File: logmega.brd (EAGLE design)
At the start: 163.8 x 97.2 mm, 94 parts, among them IC1 LTC4412, IC2 4050D, IC3 ATMEGA2560-16AU, IC4 4050D, J1 POWER_JACKPTH, M0R1 ?K, M0R2 ?K, M1 FDG6342L, M1C1 ?uF, M1R1 ?K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

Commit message: begin 083_rev2
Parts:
- C11: value 100n -> 0.1uF
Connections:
- net VCC_SW_SHIELD1: no longer U$7.IOREF
- net VCC_SW_SHIELD2: now also U$7.IOREF
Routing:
- net VCC_SW_SHIELD1: track 109.2 -> 23.9 mm, vias 3 -> 0
- net VCC_SW_SHIELD2: track 16.0 -> 25.1 mm
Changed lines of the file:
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@@
 <text x="138.5825" y="22.2025" size="0.6096" layer="21">TM</text>
 <text x="156.9085" y="81.6102" size="0.6096" layer="21" rot="R90">TM</text>
-<text x="153.9875" y="22.5425" size="0.8128" layer="21" rot="R180">1</text>
+<text x="153.4287" y="21.7043" size="0.8128" layer="21" rot="R270">1</text>
 <text x="144.145" y="36.195" size="0.8128" layer="21">v. 0.8.3</text>
 <wire x1="160.9725" y1="0" x2="163.83" y2="2.8575" width="0" layer="20" curve="90"/>
@@
 <text x="119.65" y="7.875" size="1.27" layer="21" rot="R90">44</text>
 <text x="123.15" y="7.875" size="1.27" layer="21" rot="R90">45</text>
+<circle x="152.8064" y="21.9456" radius="0.1016" width="0.4064" layer="21"/>
 </plain>
 <attributes>
@@
 <attribute name="VALUE" x="153.6887" y="1.8149" size="1.778" layer="27" rot="R90"/>
 </element>
-<element name="C_RESET" library="resistor" package="C0603" value="0.1uF" x="111.905" y="53.5625" smashed="yes" rot="R270"/>
+<element name="C_RESET" library="resistor" package="C0603" value="0.1uF" x="111.905" y="53.5625" smashed="yes" rot="R270">
+<attribute name="VALUE" x="109.1618" y="55.7723" size="1.27" layer="27" rot="R270"/>
+</element>
 <element name="R_REF_A0" library="resistor" package="0207/10" value="Therm" x="55.88" y="75.2475" smashed="yes" rot="R90">
 <attribute name="NAME" x="56.2991" y="72.4027" size="0.8128" layer="21" ratio="10" rot="R90"/>
@@
 <attribute name="VALUE" x="151.257" y="16.256" size="0.8128" layer="27" rot="R90"/>
 </element>
-<element name="C11" library="SmartPrj" package="C0603-ROUND" value="100n" x="27.6225" y="36.83" smashed="yes" rot="R180">
+<element name="C11" library="SmartPrj" package="C0603-ROUND" value="0.1uF" x="27.6225" y="36.83" smashed="yes" rot="R180">
 <attribute name="VALUE" x="24.638" y="34.8615" size="1.27" layer="27" rot="R270"/>
 </element>
@@
 <attribute name="VALUE" x="27.6225" y="52.705" size="0.8128" layer="27" rot="R270"/>
 </element>
-<element name="CBB" library="SparkFun" package="EIA3216" value="10uF" x="17.78" y="25.7175" rot="R180"/>
-<element name="RTC_INT_PU" library="rcl" package="R0603" value="10K" x="39.37" y="25.4" smashed="yes" rot="R180"/>
+<element name="CBB" library="SparkFun" package="EIA3216" value="10uF" x="17.78" y="25.7175" smashed="yes" rot="R180">
+<attribute name="NAME" x="19.2024" y="24.3365" size="0.4064" layer="25" rot="R180"/>
+<attribute name="VALUE" x="15.5433" y="24.1792" size="0.8128" layer="27" rot="R270"/>
+</element>
+<element name="RTC_INT_PU" library="rcl" package="R0603" value="10K" x="39.37" y="25.4" smashed="yes" rot="R180">
+<attribute name="VALUE" x="40.6146" y="27.813" size="1.27" layer="27" rot="R180"/>
+</element>
 <element name="RTC_RST_PU" library="rcl" package="R0603" value="10K" x="43.4975" y="25.0825" smashed="yes" rot="R90"/>
 <element name="VCC_VDIV_1" library="rcl" package="R0603" value="1M" x="92.3925" y="55.5625" smashed="yes" rot="R90"/>
@@
 <wire x1="77.1652" y1="50.1396" x2="76.6572" y2="49.6316" width="0.2032" layer="16"/>
 <wire x1="80.7212" y1="50.1396" x2="77.1652" y2="50.1396" width="0.2032" layer="16"/>
-<wire x1="82.2452" y1="51.6636" x2="80.7212" y2="50.1396" width="0.2032" layer="1"/>
-<wire x1="82.2452" y1="52.8828" x2="82.2452" y2="51.6636" width="0.2032" layer="1"/>
-<wire x1="83.0072" y1="53.6448" x2="82.2452" y2="52.8828" width="0.2032" layer="1"/>
+<wire x1="83.0072" y1="53.6448" x2="82.6516" y2="53.2892" width="0.2032" layer="1"/>
+<wire x1="82.6516" y1="53.2892" x2="82.2452" y2="52.8828" width="0.2032" layer="1"/>
 <wire x1="85.3948" y1="53.6448" x2="83.0072" y2="53.6448" width="0.2032" layer="1"/>
 <wire x1="85.3948" y1="54.4576" x2="85.3948" y2="53.6448" width="0.2032" layer="1"/>
@@
 <via x="102.87" y="55.7276" extent="1-16" drill="0.508"/>
 <via x="129.9464" y="82.804" extent="1-16" drill="0.508"/>
+<wire x1="80.7212" y1="50.1396" x2="80.7212" y2="51.3588" width="0.2032" layer="1"/>
+<wire x1="80.7212" y1="51.3588" x2="82.2452" y2="52.8828" width="0.2032" layer="1"/>
 </signal>
 <signal name="D41-SHIELD1_CS">
@@
 <wire x1="34.6075" y1="18.7175" x2="35.8625" y2="17.4625" width="0.6096" layer="16"/>
 <contactref element="U$9" pad="IOREF"/>
-<contactref element="U$7" pad="IOREF"/>
 <wire x1="21.9964" y1="18.8468" x2="20.6248" y2="17.4752" width="0.4064" layer="16"/>
 <wire x1="26.67" y1="18.8468" x2="21.9964" y2="18.8468" width="0.4064" layer="16"/>
@@
 <wire x1="20.6248" y1="17.4752" x2="20.6225" y2="17.4625" width="0.4064" layer="16"/>
 <wire x1="27.8892" y1="17.6276" x2="28.2425" y2="17.4625" width="0.4064" layer="16"/>
-<wire x1="82.7532" y1="51.6128" x2="83.4644" y2="52.324" width="0.4064" layer="1"/>
-<wire x1="82.7532" y1="51.0032" x2="82.7532" y2="51.6128" width="0.4064" layer="1"/>
-<wire x1="81.6864" y1="49.9364" x2="82.7532" y2="51.0032" width="0.4064" layer="1"/>
-<wire x1="81.6864" y1="38.5064" x2="81.6864" y2="49.9364" width="0.4064" layer="1"/>
-<wire x1="81.2292" y1="38.9636" x2="81.6864" y2="38.5064" width="0.4064" layer="16"/>
-<wire x1="65.7352" y1="38.9636" x2="81.2292" y2="38.9636" width="0.4064" layer="16"/>
-<wire x1="62.8904" y1="36.1188" x2="65.7352" y2="38.9636" width="0.4064" layer="16"/>
-<wire x1="58.2676" y1="36.1188" x2="62.8904" y2="36.1188" width="0.4064" layer="16"/>
-<wire x1="56.8452" y1="34.6964" x2="58.2676" y2="36.1188" width="0.4064" layer="1"/>
-<wire x1="56.8452" y1="22.1488" x2="56.8452" y2="34.6964" width="0.4064" layer="1"/>
-<wire x1="58.166" y1="20.828" x2="56.8452" y2="22.1488" width="0.4064" layer="1"/>
-<wire x1="58.166" y1="14.732" x2="58.166" y2="20.828" width="0.4064" layer="1"/>
-<wire x1="57.7088" y1="15.1892" x2="58.166" y2="14.732" width="0.4064" layer="16"/>
-<wire x1="38.2524" y1="15.1892" x2="57.7088" y2="15.1892" width="0.4064" layer="16"/>
-<wire x1="36.1188" y1="17.3228" x2="38.2524" y2="15.1892" width="0.4064" layer="16"/>
-<wire x1="83.4644" y1="52.324" x2="83.5025" y2="52.3725" width="0.4064" layer="1"/>
-<wire x1="36.1188" y1="17.3228" x2="35.8625" y2="17.4625" width="0.4064" layer="16"/>
-<via x="81.6864" y="38.5064" extent="1-16" drill="0.8"/>
-<via x="58.2676" y="36.1188" extent="1-16" drill="0.8"/>
-<via x="58.166" y="14.732" extent="1-16" drill="0.8"/>
 </signal>
 <signal name="VCC_SW_SHIELD2" class="3">
@@
 <wire x1="84.8868" y1="37.1475" x2="84.8868" y2="43.3324" width="0.4064" layer="1"/>
 <wire x1="83.5152" y1="44.704" x2="83.5025" y2="44.7525" width="0.4064" layer="1"/>
+<contactref element="U$7" pad="IOREF"/>
+<wire x1="83.5025" y1="44.7525" x2="81.788" y2="46.467" width="0.4064" layer="1"/>
+<wire x1="81.788" y1="46.467" x2="81.788" y2="50.9016" width="0.4064" layer="1"/>
+<wire x1="81.788" y1="50.9016" x2="83.2589" y2="52.3725" width="0.4064" layer="1"/>
+<wire x1="83.2589" y1="52.3725" x2="83.5025" y2="52.3725" width="0.4064" layer="1"/>
 </signal>
 </signals>

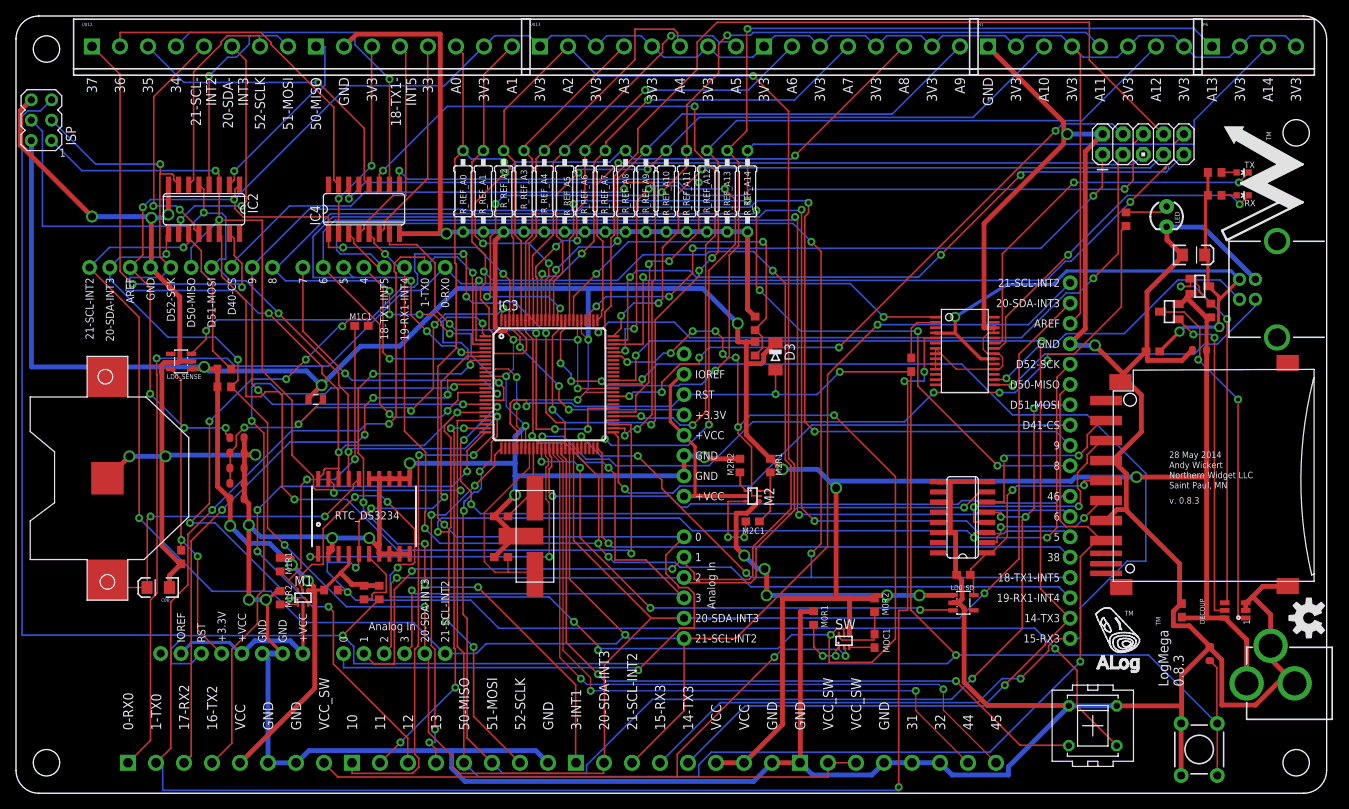
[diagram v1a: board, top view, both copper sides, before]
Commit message: Load switch resistors and capacitors labeled (#11) and CR2032 replaced with part with keepout (#3)
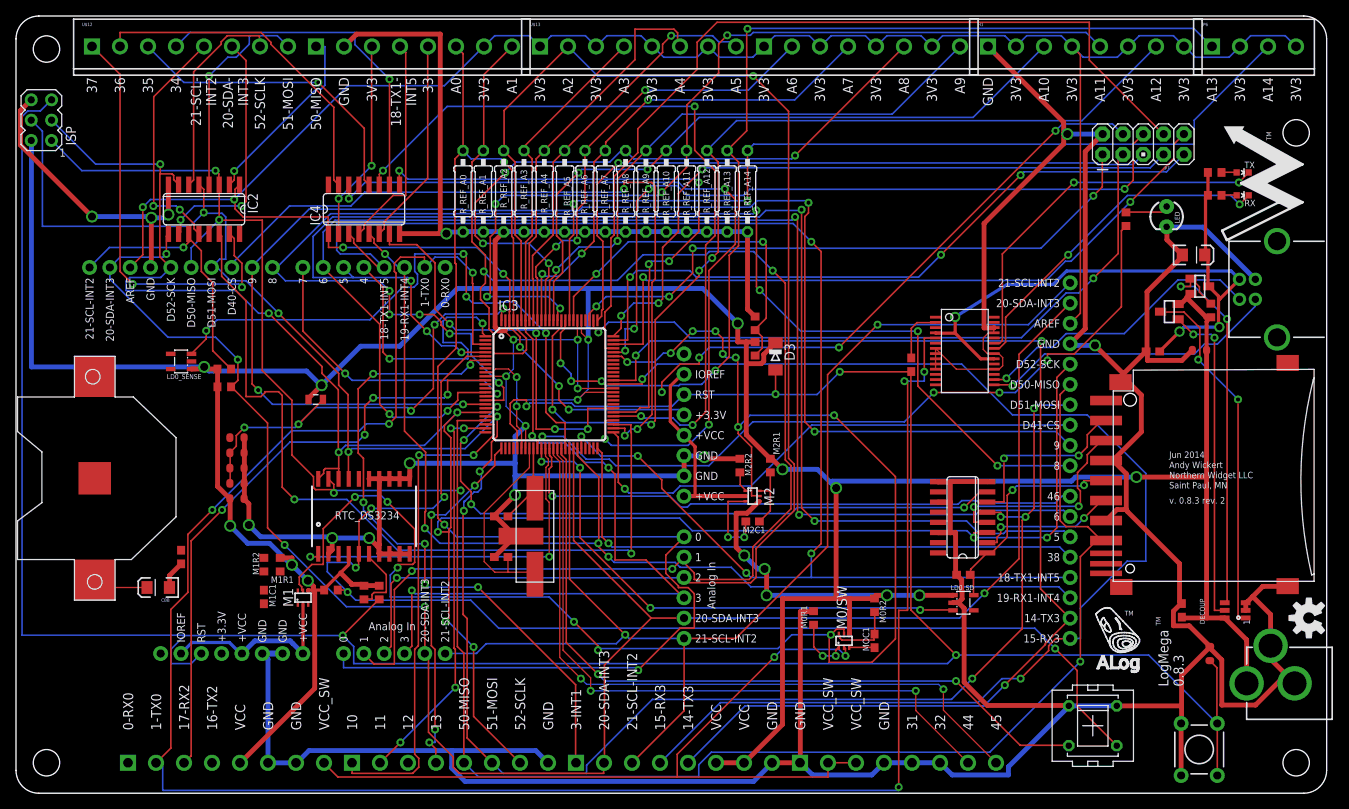
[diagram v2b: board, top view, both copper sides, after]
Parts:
- CLOCK_BATT: device adafruit:CR2032-SMD -> awickert:CR2032-SMD
- M0R1, M0R2, M1R1, M1R2, M2R1, M2R2: value ?K -> 10K
- M1C1, M2C1, MOC1: value ?uF -> 0.1uF
- moved M1C1 36.0 mm to (31.0, 24.5), turned to 270 degrees
- moved M1R2 4.60 mm to (31.0, 28.6)
- moved CLOCK_BATT 1.59 mm to (9.84, 39.4)
- renumbered SW to M0/SW
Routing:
- net D0-RX0: track 166.8 -> 0.00 mm, vias 3 -> 0
- net GND: track 873.1 -> 787.2 mm, vias 22 -> 17
- net D16-TX2: track 80.9 -> 0.00 mm, vias 2 -> 0
- net D21-SCL-INT2: track 267.8 -> 188.7 mm, vias 4 -> 3
- net D12: track 74.6 -> 0.00 mm, vias 4 -> 0
- net +3V3: track 358.9 -> 289.5 mm, vias 12 -> 7
- net N$16: track 58.8 -> 0.00 mm, vias 6 -> 0
- net N$15: track 40.7 -> 0.00 mm, vias 2 -> 0
- net BAT: track 42.7 -> 6.71 mm, vias 2 -> 0
- net D30: track 79.5 -> 73.3 mm, vias 5 -> 4
- net N$12: track 2.24 -> 0.00 mm
- net D34: track 76.0 -> 76.6 mm
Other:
- board text added: "Jun 2014"
- board text added: "v. 0.8.3 rev. 2"
- board text removed: "28 May 2014"
- board text removed: "v. 0.8.3"

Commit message: Moved 'Log Now' and 'Reset' buttons (Issue #1)
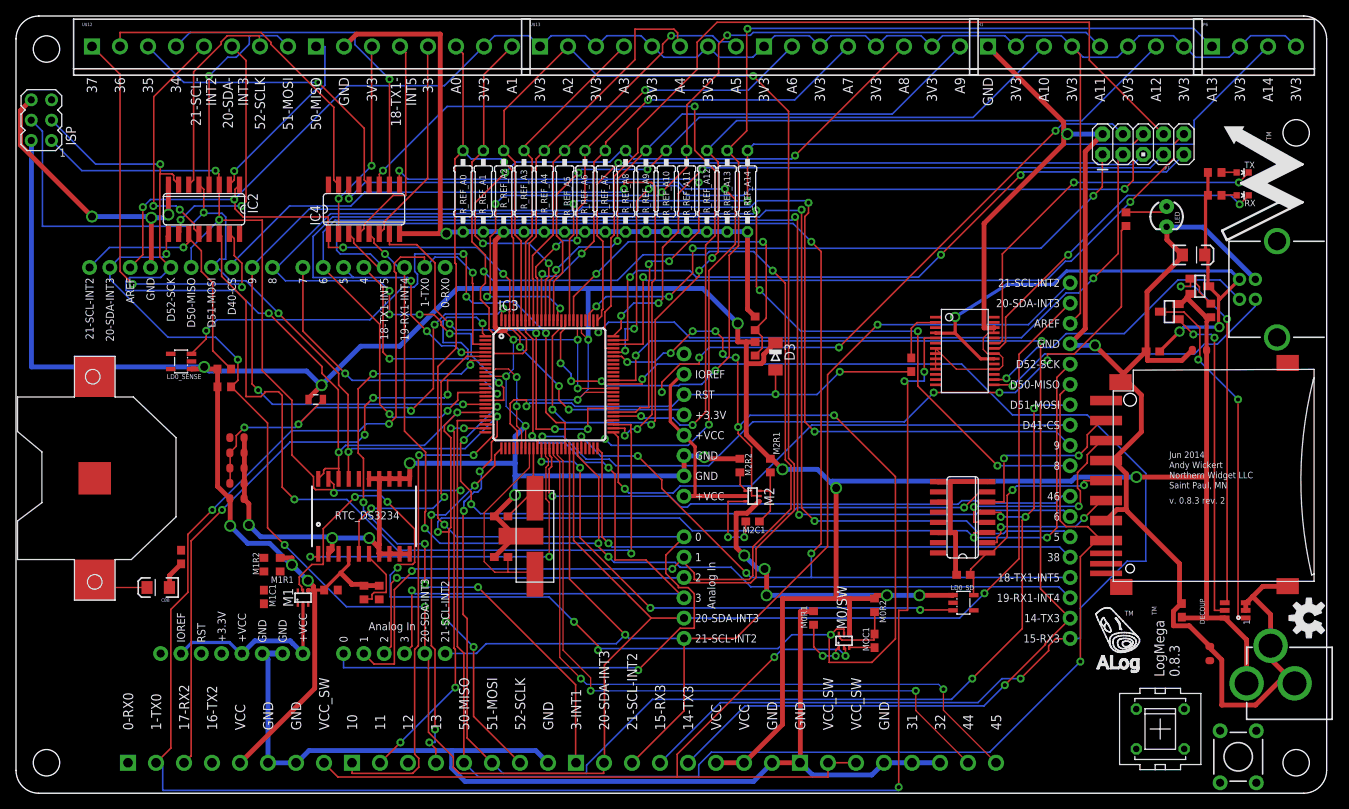
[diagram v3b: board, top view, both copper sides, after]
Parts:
- moved MANUAL_LOG 8.44 mm to (143.0, 8.03)
- moved S2 4.96 mm to (152.8, 4.56)
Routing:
- net RESET: track 355.3 -> 62.3 mm, vias 5 -> 3
- net D2-INT0-CLOCK: track 156.1 -> 37.5 mm, vias 5 -> 2
- net D43_MANUAL_LOG: track 92.7 -> 0.04 mm, vias 2 -> 0
- net GND: track 787.2 -> 705.1 mm

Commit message: Multiple silkscreen and value label changes: #13 #16 #18 #20
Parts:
- C3, C4, C5, C6: value 100n -> 0.1uF
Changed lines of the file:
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@@
 <attribute name="VALUE" x="69.215" y="72.9869" size="1.27" layer="27" ratio="10" rot="R90"/>
 </element>
-<element name="C3" library="SmartPrj" package="C0603-ROUND" value="100n" x="27.6225" y="44.45" smashed="yes"/>
-<element name="C6" library="SmartPrj" package="C0603-ROUND" value="100n" x="27.6225" y="38.735" smashed="yes"/>
+<element name="C3" library="SmartPrj" package="C0603-ROUND" value="0.1uF" x="27.6225" y="44.45" smashed="yes"/>
+<element name="C6" library="SmartPrj" package="C0603-ROUND" value="0.1uF" x="27.6225" y="38.735" smashed="yes"/>
 <element name="IC3" library="SmartPrj" package="TQFP100" value="ATMEGA2560-16AU" x="66.675" y="51.1175"/>
-<element name="C5" library="SmartPrj" package="C0603-ROUND" value="100n" x="27.6225" y="40.64" smashed="yes"/>
-<element name="C4" library="SmartPrj" package="C0603-ROUND" value="100n" x="27.6225" y="42.545" smashed="yes"/>
+<element name="C5" library="SmartPrj" package="C0603-ROUND" value="0.1uF" x="27.6225" y="40.64" smashed="yes"/>
+<element name="C4" library="SmartPrj" package="C0603-ROUND" value="0.1uF" x="27.6225" y="42.545" smashed="yes"/>
 <element name="C1" library="SmartPrj" package="C0603-ROUND" value="22pF" x="149.225" y="17.4625" smashed="yes" rot="R90">
 <attribute name="VALUE" x="151.257" y="16.256" size="0.8128" layer="27" rot="R90"/>
 </element>
 <element name="C11" library="SmartPrj" package="C0603-ROUND" value="0.1uF" x="27.6225" y="36.83" smashed="yes" rot="R180">
-<attribute name="VALUE" x="24.638" y="34.8615" size="1.27" layer="27" rot="R270"/>
+<attribute name="VALUE" x="29.5148" y="42.8879" size="1.27" layer="27" rot="R270"/>
 </element>
 <element name="D3" library="diode" package="MINIMELF" value="CD1206-S01575" x="94.9325" y="54.61" rot="R270"/>
